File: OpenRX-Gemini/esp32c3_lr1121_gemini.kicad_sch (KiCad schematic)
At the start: 67 parts, among them T1 0900PC16J0042001E, T2 0900PC16J0042001E, U1 OW7EL89CENUYO3YLC-32M, U10 RFX2401C, U11 SKY13414-485LF, U2 LR1121IMLTRT, U3 ESP32-C3FH4, U4 TS2306A 240GF MSM 9_C2976675, U5 RFX2401C, U6 TLV75533PDQNR, U7 SKY13414-485LF, U8 OW7EL89CENUYO3YLC-32M, U9 LR1121IMLTRT, X1 CJ17-400001010B20

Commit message: initial routing for all
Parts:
- removed C19, C30: 0.3pF, Capacitor_SMD:C_0201_0603Metric, symbol Device:C
- removed C21, C31: 220pF, Capacitor_SMD:C_0201_0603Metric, symbol Device:C
- removed C23, C32: 1uF, Capacitor_SMD:C_0201_0603Metric, symbol Device:C
- removed C5: 100nF, Capacitor_SMD:C_0201_0603Metric, symbol Device:C
- removed JP1, JP2: U.FL-R-SMT-1(80), OpenRX-Shared:RF-SMD_FRF05002-JSS103M, symbol OpenRX-Shared:U.FL-R-SMT-1(80)
- removed T1, T2: 0900PC16J0042001E, OpenRX-Shared:FILTER-SMD_10P-L2.0-W1.6-BL, symbol OpenRX-Shared:0900PC16J0042001E
- removed U10, U5: RFX2401C, OpenRX-Shared:QFN-16_L3.0-W3.0-P0.50-BL-EP1.7, symbol OpenRX-Shared:RFX2401C
- removed U11, U7: SKY13414-485LF, OpenRX-Shared:QFN-14_L2.0-W2.0-P0.45-BL-EP, symbol OpenRX-Shared:SKY13414-485LF
- removed U8: OW7EL89CENUYO3YLC-32M, OpenRX-Shared:OSC-SMD_4P-L2.0-W1.6-BL_TXC_7Z, symbol OpenRX-Shared:OW7EL89CENUYO3YLC-32M
- removed USB1, USB2: 2450FM07D0034, OpenRX-Shared:FILTER-SMD_4P-L1.0-W0.5-L_DEA102700LT-XXX, symbol OpenRX-Shared:DEA102700LT-6307A2
- added C42, C45: 0.3pF, Capacitor_SMD:C_0201_0603Metric, symbol Device:C
- added C43, C46: 220pF, Capacitor_SMD:C_0201_0603Metric, symbol Device:C
- added C44, C47: 1uF, Capacitor_SMD:C_0201_0603Metric, symbol Device:C
- added FL4, FL5: 2450FM07D0034T, OpenRX-Shared:FILTER-SMD_4P-L1.0-W0.5-L, symbol OpenRX-Shared:2450FM07D0034T
- added H1: MountingHole, MountingHole:MountingHole_3.2mm_M3_Pad, symbol Mechanical:MountingHole
- added JP4, JP5: U.FL-R-SMT-1(80), OpenRX-Shared:RF-SMD_FRF05002-JSS103M, symbol OpenRX-Shared:U.FL-R-SMT-1(80)
- added R10, R9: 680R, Resistor_SMD:R_0201_0603Metric, symbol Device:R
- added R11: 10k, Resistor_SMD:R_0201_0603Metric, symbol Device:R
- added T4, T5: 0900PC16J0042001E, OpenRX-Shared:FILTER-SMD_10P-L2.0-W1.6-BL, symbol OpenRX-Shared:0900PC16J0042001E
- added U15, U17: RFX2401C, OpenRX-Shared:QFN-16_L3.0-W3.0-P0.50-BL-EP1.7, symbol OpenRX-Shared:RFX2401C
- added U16, U18: SKY13414-485LF, OpenRX-Shared:QFN-14_L2.0-W2.0-P0.45-BL-EP, symbol OpenRX-Shared:SKY13414-485LF
- C1, C4: LCSC Part (none) -> C62164
- C10, C11, C12, C13, C15, C17, C18, C24, C25, C26, C29, C3, C7: LCSC Part (none) -> C76939
- C14, C22: LCSC Part (none) -> C15525
- C16, C2, C20, C6: LCSC Part (none) -> C76935
- C27, C8: LCSC C20069240 -> C76921; LCSC Part (none) -> C76921
- C28, C9: LCSC Part (none) -> C23733
- L1: LCSC Part (none) -> C206441
- L2, L3: LCSC C6808014 -> C1035; LCSC Part (none) -> C1035
- R1, R2, R4, R5, R6, R7: LCSC Part (none) -> C106225
- R3, R8: LCSC Part (none) -> C274342
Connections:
- net +3V3: now also C43.1, C44.1, C46.1, C47.1, R11.1, U15.14 (VDD), U15.16 (VDD), U16.4 (VDD), U17.14 (VDD), U17.16 (VDD), U18.4 (VDD)
- net BUSY2: now also R11.2
- net DIO7-1: now also U18.5 (V3)
- net DIO7-2: now also U16.5 (V3)
- net DIO8-1: now also U18.6 (V2)
- net DIO8-2: now also U16.6 (V2)
- net GND: now also C42.2, C43.2, C44.2, C45.2, C46.2, C47.2, FL4.2 (GND), FL4.4 (GND), FL5.2 (GND), FL5.4 (GND), JP4.2 (GND), JP4.3 (GND), JP5.2 (GND), JP5.3 (GND), T4.10 (GND), T4.5 (GND), T4.7 (GND), T5.10 (GND), T5.5 (GND), T5.7 (GND), U15.1 (GND), U15.11 (GND), U15.12 (GND), U15.15 (GND), U15.17 (EP), U15.2 (GND), U15.3 (GND), U15.7 (GND), U15.8 (GND), U15.9 (GND), U16.15 (EP), U16.7 (V1), U17.1 (GND), U17.11 (GND), U17.12 (GND), U17.15 (GND), U17.17 (EP), U17.2 (GND), U17.3 (GND), U17.7 (GND), U17.8 (GND), U17.9 (GND), U18.15 (EP), U18.7 (V1)
- net MISO: now also R10.2, R9.2; no longer U2.21 (DIO4), U9.21 (DIO4)
- net RXEN1: now also U17.6 (RXEN)
- net RXEN2: now also U15.6 (RXEN)
- net TXEN1: now also U17.5 (TXEN)
- net TXEN2: now also U15.5 (TXEN)
- net at U2.3 (VTCXO): no longer U1.4 (VDD)
- net at U9.26 (RFIO_HF): now also FL5.1 (IN)
- net VTCXO: now reaches C25.2, U9.3 (VTCXO)
- net VTCXO: now also U1.4 (VDD)
- net XTA: now reaches R3.2, U1.3 (OUTPUT)
- net XTA: now also R8.2
- net at U2.26 (RFIO_HF): now also FL4.1 (IN)
- net at U2.32 (RFO_HP_LF): now also T4.1 (RFO_HP_LF)
- net at U2.31 (RFO_LP_LF): now also T4.2 (RFO_LP_LF)
- net at U2.30 (RFI_P_LF0): now also T4.3 (RFI_P_LFO)
- net at U2.29 (RFI_N_LF0): now also T4.4 (RFI_N_LFO)
- net at U9.32 (RFO_HP_LF): now also T5.1 (RFO_HP_LF)
- net at U9.31 (RFO_LP_LF): now also T5.2 (RFO_LP_LF)
- net at U9.30 (RFI_P_LF0): now also T5.3 (RFI_P_LFO)
- net at U9.29 (RFI_N_LF0): now also T5.4 (RFI_N_LFO)
- new net: R10.1, U9.21 (DIO4)
- new net: FL5.3 (OUT), U17.4 (TXRX)
- new net: C42.1, U15.10 (ANT), U16.10 (RF4)
- new net: JP4.1 (SIG), U16.13 (ANT)
- new net: T4.9 (TX_HP), U16.2 (RF3)
- new net: T4.6 (RX), U16.3 (RF1)
- new net: R9.1, U2.21 (DIO4)
- new net: C45.1, U17.10 (ANT), U18.10 (RF4)
- new net: T5.6 (RX), U18.3 (RF1)
- new net: T5.9 (TX_HP), U18.2 (RF3)
- new net: FL4.3 (OUT), U15.4 (TXRX)
- new net: JP5.1 (SIG), U18.13 (ANT)
- no-connect marks 26 -> 41
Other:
- moved on the sheet: C12, D1, R6, U1

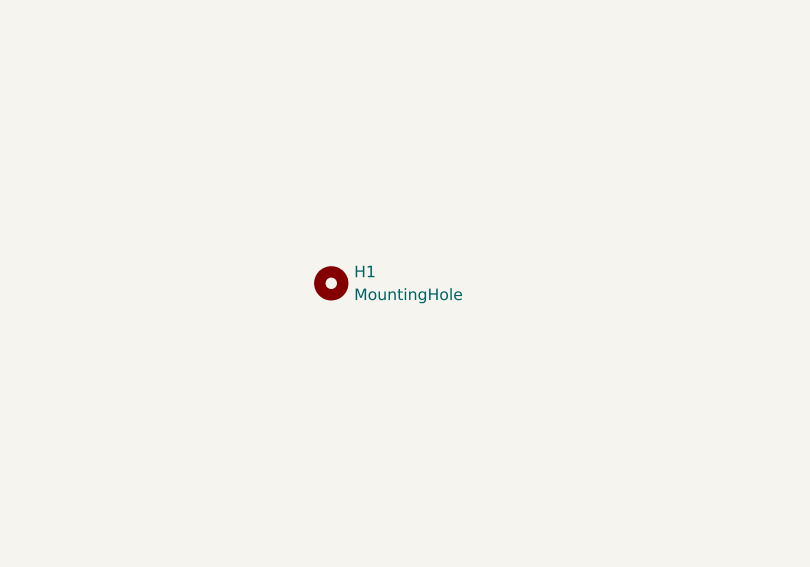
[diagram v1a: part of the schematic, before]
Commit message: switch to 0.2mm vias
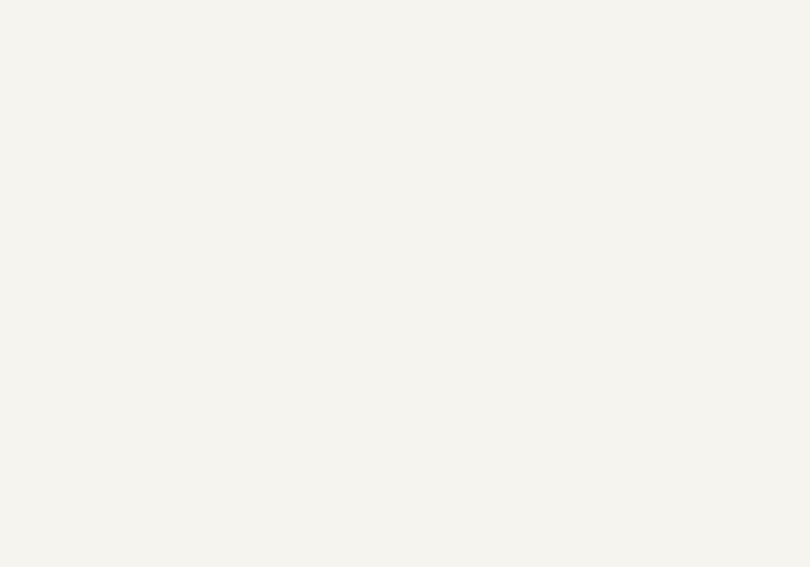
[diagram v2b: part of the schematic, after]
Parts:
- removed H1: MountingHole, MountingHole:MountingHole_3.2mm_M3_Pad, symbol Mechanical:MountingHole
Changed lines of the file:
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@@
-	)
-	(symbol
-		(lib_id "Mechanical:MountingHole")
-		(at 273.05 71.12 0)
-		(unit 1)
-		(body_style 1)
-		(exclude_from_sim no)
-		(in_bom no)
-		(on_board yes)
-		(in_pos_files yes)
-		(dnp no)
-		(fields_autoplaced yes)
-		(property "Reference" "H1"
-			(at 275.59 69.8499 0)
-			(show_name no)
-			(do_not_autoplace no)
-			(effects
-				(font
-					(size 1.27 1.27)
-				)
-				(justify left)
-			)
-		)
-		(property "Value" "MountingHole"
-			(at 275.59 72.3899 0)
-			(show_name no)
-			(do_not_autoplace no)
-			(effects
-				(font
-					(size 1.27 1.27)
-				)
-				(justify left)
-			)
-		)
-		(property "Footprint" "MountingHole:MountingHole_3.2mm_M3_Pad"
-			(at 273.05 71.12 0)
-			(hide yes)
-			(show_name no)
-			(do_not_autoplace no)
-			(effects
-				(font
-					(size 1.27 1.27)
-				)
-			)
-		)
-		(property "Datasheet" ""
-			(at 273.05 71.12 0)
-			(hide yes)
-			(show_name no)
-			(do_not_autoplace no)
-			(effects
-				(font
-					(size 1.27 1.27)
-				)
-			)
-		)
-		(property "Description" "Mounting Hole without connection"
-			(at 273.05 71.12 0)
-			(hide yes)
-			(show_name no)
-			(do_not_autoplace no)
-			(effects
-				(font
-					(size 1.27 1.27)
-				)
-			)
-		)
-		(instances
-			(project "OpenRX-Gemini"
-				(path "/c2d3e4f5-a6b7-8901-cdef-234567890abc/a1b2c3d4-e5f6-7890-abcd-ef0123456789"
-					(reference "H1")
-					(unit 1)
-				)
-			)
-		)
 	)
 	(symbol
